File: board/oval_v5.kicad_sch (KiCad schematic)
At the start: 131 parts, among them J1 HDR-5x1, J10 HDR-4x1, J11 HDR-4x1, J12 HDR-4x1, J13 HDR-4x1, J14 HDR-4x1, J15 HDR-4x1, J16 HDR-4x1, J17 HDR-4x1, J18 Conn_Coaxial, J19 Conn_01x02, J2 HDR-4x1, J20 Conn_01x02, J21 Conn_02x02_Counter_Clockwise, J22 HDR-2x1, J23 HDR-2x1, J25 Conn_01x06, J3 HDR-4x1, J4 Conn_01x06, J5 Micro_SD_Card, J6 Conn_01x02, J7 HDR-4x1, J8 Conn_01x08, J9 HDR-4x1, P1 USB_C_Plug_USB2.0, Q1 Q_PMOS_GSD, Q2 MMBT3904, Q3 MMBT3904, SW1 SW_DIP_x02, SW2 SW_DIP_x02, U1 RV-8803, U10 SiP32431DR3, U11 SiP32431DR3, U12 SiP32431DR3, U13 SiP32431DR3, U14 SiP32431DR3, U16 PCA9548APW, U17 SiP32431DR3, U18 PCA9555PW, U2 ESP32-S3-WROOM-1, U3 TMP117xxDRV, U4 RFM95W-915S2, U7 MAX3485, U8 AP7361C-33E, U9 AP7361C-33E

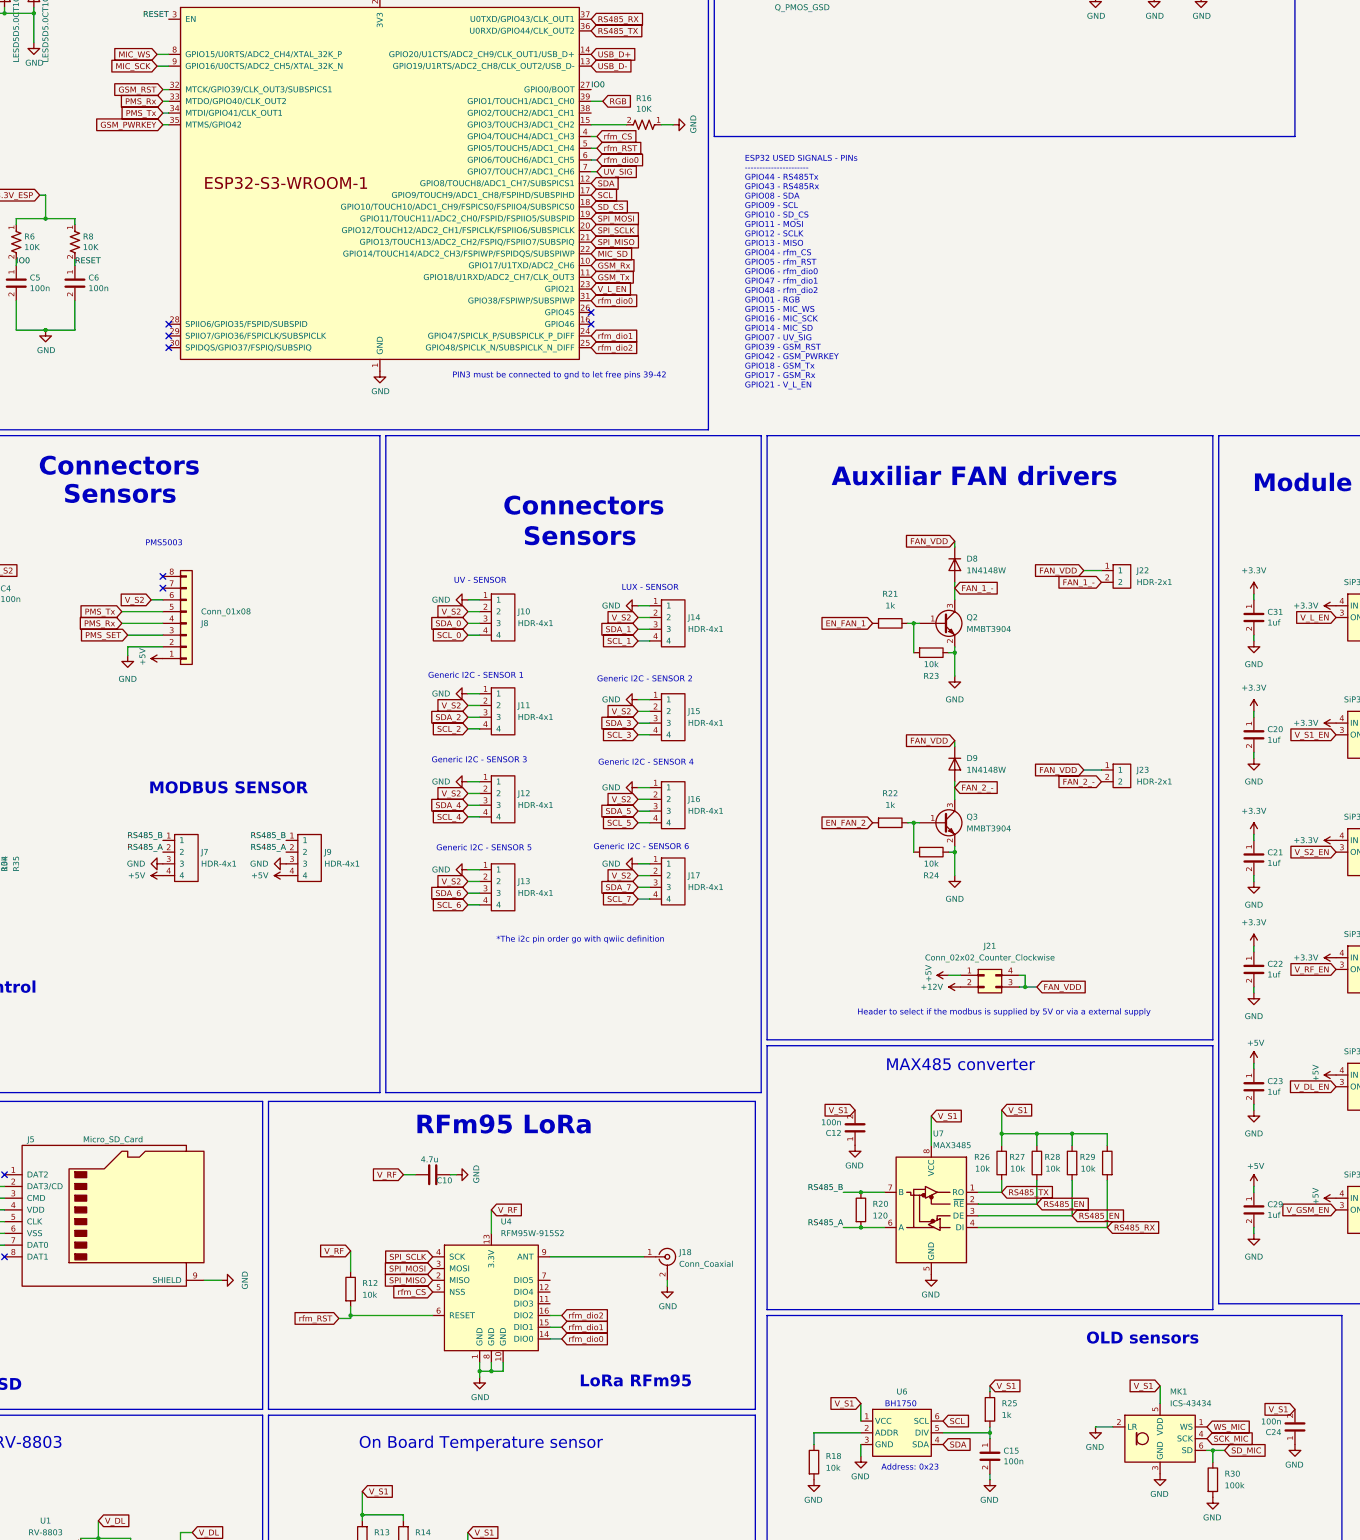
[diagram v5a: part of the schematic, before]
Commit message: routing pads
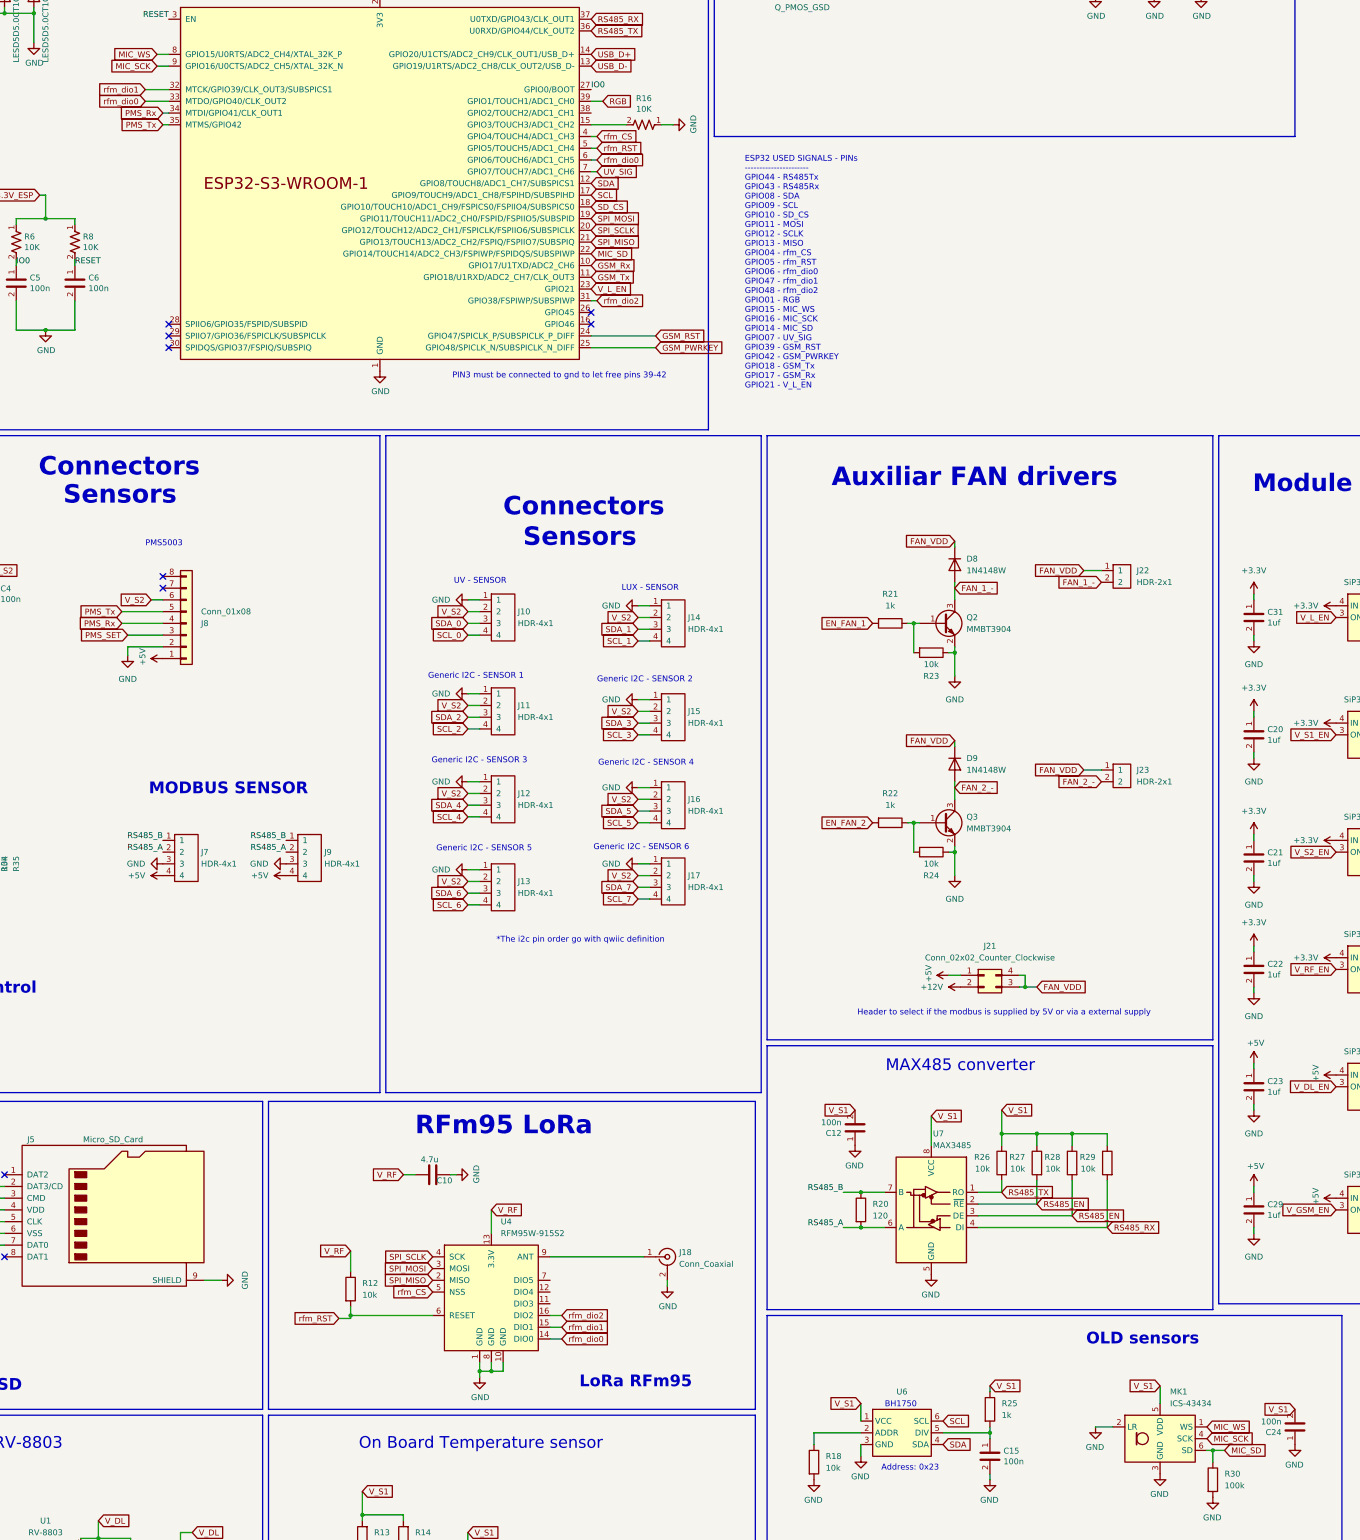
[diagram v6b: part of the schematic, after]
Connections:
- net SCK_MIC is gone; now on net MIC_SCK: MK1.4 (SCK)
- net SD_MIC is gone; now on net MIC_SD: MK1.6 (SD), R30.1
- net WS_MIC is gone; now on net MIC_WS: MK1.1 (WS)
- net GSM_PWRKEY: now also U2.25 (GPIO48/SPICLK_N/SUBSPICLK_N_DIFF); no longer U2.35 (MTMS/GPIO42)
- net GSM_RST: now also U2.24 (GPIO47/SPICLK_P/SUBSPICLK_P_DIFF); no longer U2.32 (MTCK/GPIO39/CLK_OUT3/SUBSPICS1)
- net PMS_Rx: now also U2.34 (MTDI/GPIO41/CLK_OUT1); no longer U2.33 (MTDO/GPIO40/CLK_OUT2)
- net PMS_Tx: now also U2.35 (MTMS/GPIO42); no longer U2.34 (MTDI/GPIO41/CLK_OUT1)
- net rfm_dio0: now also U2.33 (MTDO/GPIO40/CLK_OUT2); no longer U2.31 (GPIO38/FSPIWP/SUBSPIWP)
- net rfm_dio1: now also U2.32 (MTCK/GPIO39/CLK_OUT3/SUBSPICS1); no longer U2.24 (GPIO47/SPICLK_P/SUBSPICLK_P_DIFF)
- net rfm_dio2: now also U2.31 (GPIO38/FSPIWP/SUBSPIWP); no longer U2.25 (GPIO48/SPICLK_N/SUBSPICLK_N_DIFF)
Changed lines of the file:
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@@
 	(wire
 		(pts
-			(xy 95.25 93.98) (xy 96.52 93.98)
+			(xy 91.44 93.98) (xy 96.52 93.98)
 		)
 		(stroke
@@
 	(wire
 		(pts
+			(xy 187.96 144.78) (xy 201.93 144.78)
+		)
+		(stroke
+			(width 0)
+			(type default)
+		)
+	)
+	(wire
+		(pts
 			(xy 31.75 392.43) (xy 31.75 389.89)
 		)
@@
 	(wire
 		(pts
+			(xy 189.23 137.16) (xy 187.96 137.16)
+		)
+		(stroke
+			(width 0)
+			(type default)
+		)
+	)
+	(wire
+		(pts
 			(xy 331.47 302.26) (xy 331.47 303.53)
 		)
@@
 	(wire
 		(pts
+			(xy 187.96 147.32) (xy 201.93 147.32)
+		)
+		(stroke
+			(width 0)
+			(type default)
+		)
+	)
+	(wire
+		(pts
 			(xy 93.98 83.82) (xy 96.52 83.82)
 		)
@@
 	(wire
 		(pts
-			(xy 95.25 91.44) (xy 96.52 91.44)
+			(xy 91.44 91.44) (xy 96.52 91.44)
 		)
 		(stroke
@@
 		)
 	)
-	(global_label "V_DL"
+	(global_label "rfm_dio1"
 		(shape input)
-		(at 81.28 401.32 0)
+		(at 91.44 91.44 180)
 		(fields_autoplaced yes)
 		(effects
@@
 				(size 1.27 1.27)
 			)
-			(justify left)
+			(justify right)
 		)
 		(property "Intersheetrefs" "${INTERSHEET_REFS}"
-			(at 88.6195 401.32 0)
+			(at 80.1697 91.44 0)
 			(effects
 				(font
 					(size 1.27 1.27)
 				)
-				(justify left)
+				(justify right)
 				(hide yes)
 			)
 		)
 	)
-	(global_label "rfm_dio0"
+	(global_label "V_DL"
 		(shape input)
-		(at 187.96 137.16 0)
+		(at 81.28 401.32 0)
 		(fields_autoplaced yes)
 		(effects
@@
 		)
 		(property "Intersheetrefs" "${INTERSHEET_REFS}"
-			(at 199.2303 137.16 0)
+			(at 88.6195 401.32 0)
 			(effects
 				(font
@@
 		)
 	)
-	(global_label "SCK_MIC"
+	(global_label "MIC_SCK"
 		(shape input)
 		(at 321.31 383.54 0)
@@
 		)
 	)
+	(global_label "PMS_Rx"
+		(shape input)
+		(at 95.25 96.52 180)
+		(fields_autoplaced yes)
+		(effects
+			(font
+				(size 1.27 1.27)
+			)
+			(justify right)
+		)
+		(property "Intersheetrefs" "${INTERSHEET_REFS}"
+			(at 85.0682 96.52 0)
+			(effects
+				(font
+					(size 1.27 1.27)
+				)
+				(justify right)
+				(hide yes)
+			)
+		)
+	)
 	(global_label "V_S1"
 		(shape input)
@@
 		)
 	)
-	(global_label "GSM_RST"
-		(shape input)
-		(at 95.25 91.44 180)
-		(fields_autoplaced yes)
-		(effects
-			(font
-				(size 1.27 1.27)
-			)
-			(justify right)
-		)
-		(property "Intersheetrefs" "${INTERSHEET_REFS}"
-			(at 83.9192 91.44 0)
-			(effects
-				(font
-					(size 1.27 1.27)
-				)
-				(justify right)
-				(hide yes)
-			)
-		)
-	)
 	(global_label "FAN_1_-"
 		(shape input)
@@
 		)
 	)
-	(global_label "PMS_Rx"
-		(shape input)
-		(at 95.25 93.98 180)
-		(fields_autoplaced yes)
-		(effects
-			(font
-				(size 1.27 1.27)
-			)
-			(justify right)
-		)
-		(property "Intersheetrefs" "${INTERSHEET_REFS}"
-			(at 85.0682 93.98 0)
-			(effects
-				(font
-					(size 1.27 1.27)
-				)
-				(justify right)
-				(hide yes)
-			)
-		)
-	)
 	(global_label "RGB"
 		(shape input)
@@
 		)
 	)
-	(global_label "WS_MIC"
+	(global_label "MIC_WS"
 		(shape input)
 		(at 321.31 381 0)
@@
 		)
 	)
+	(global_label "PMS_Tx"
+		(shape input)
+		(at 95.25 99.06 180)
+		(fields_autoplaced yes)
+		(effects
+			(font
+				(size 1.27 1.27)
+			)
+			(justify right)
+		)
+		(property "Intersheetrefs" "${INTERSHEET_REFS}"
+			(at 85.3706 99.06 0)
+			(effects
+				(font
+					(size 1.27 1.27)
+				)
+				(justify right)
+				(hide yes)
+			)
+		)
+	)
 	(global_label "SCL"
 		(shape input)
@@
 		)
 	)
+	(global_label "GSM_RST"
+		(shape input)
+		(at 201.93 144.78 0)
+		(fields_autoplaced yes)
+		(effects
+			(font
+				(size 1.27 1.27)
+			)
+			(justify left)
+		)
+		(property "Intersheetrefs" "${INTERSHEET_REFS}"
+			(at 213.2608 144.78 0)
+			(effects
+				(font
+					(size 1.27 1.27)
+				)
+				(justify left)
+				(hide yes)
+			)
+		)
+	)
 	(global_label "rfm_dio1"
 		(shape input)
@@
 		)
 	)
+	(global_label "GSM_PWRKEY"
+		(shape input)
+		(at 201.93 147.32 0)
+		(fields_autoplaced yes)
+		(effects
+			(font
+				(size 1.27 1.27)
+			)
+			(justify left)
+		)
+		(property "Intersheetrefs" "${INTERSHEET_REFS}"
+			(at 217.3127 147.32 0)
+			(effects
+				(font
+					(size 1.27 1.27)
+				)
+				(justify left)
+				(hide yes)
+			)
+		)
+	)
 	(global_label "SCL"
 		(shape input)
@@
 		)
 	)
-	(global_label "rfm_dio1"
-		(shape input)
-		(at 187.96 144.78 0)
-		(fields_autoplaced yes)
-		(effects
-			(font
-				(size 1.27 1.27)
-			)
-			(justify left)
-		)
-		(property "Intersheetrefs" "${INTERSHEET_REFS}"
-			(at 199.2303 144.78 0)
-			(effects
-				(font
-					(size 1.27 1.27)
-				)
-				(justify left)
-				(hide yes)
-			)
-		)
-	)
 	(global_label "SDA"
 		(shape input)
@@
 		)
 	)
-	(global_label "rfm_dio2"
-		(shape input)
-		(at 187.96 147.32 0)
-		(fields_autoplaced yes)
-		(effects
-			(font
-				(size 1.27 1.27)
-			)
-			(justify left)
-		)
-		(property "Intersheetrefs" "${INTERSHEET_REFS}"
-			(at 199.2303 147.32 0)
-			(effects
-				(font
-					(size 1.27 1.27)
-				)
-				(justify left)
-				(hide yes)
-			)
-		)
-	)
 	(global_label "SDA_5"
 		(shape input)
@@
 		)
 	)
-	(global_label "SD_MIC"
+	(global_label "MIC_SD"
 		(shape input)
 		(at 325.12 386.08 0)
@@
 		)
 	)
-	(global_label "V_RF"
+	(global_label "rfm_dio0"
 		(shape input)
-		(at 375.92 276.86 0)
+		(at 91.44 93.98 180)
 		(fields_autoplaced yes)
 		(effects
@@
 				(size 1.27 1.27)
 			)
-			(justify left)
+			(justify right)
 		)
 		(property "Intersheetrefs" "${INTERSHEET_REFS}"
-			(at 383.32 276.86 0)
+			(at 80.1697 93.98 0)
 			(effects
 				(font
 					(size 1.27 1.27)
 				)
-				(justify left)
+				(justify right)
 				(hide yes)
 			)
 		)
 	)
-	(global_label "V_S2"
+	(global_label "V_RF"
 		(shape input)
-		(at 161.29 204.47 180)
+		(at 375.92 276.86 0)
 		(fields_autoplaced yes)
 		(effects
@@
 				(size 1.27 1.27)
 			)
-			(justify right)
+			(justify left)
 		)
 		(property "Intersheetrefs" "${INTERSHEET_REFS}"
-			(at 153.8296 204.47 0)
+			(at 383.32 276.86 0)
 			(effects
 				(font
 					(size 1.27 1.27)
 				)
-				(justify right)
+				(justify left)
 				(hide yes)
 			)
 		)
 	)
-	(global_label "PMS_Tx"
+	(global_label "V_S2"
 		(shape input)
-		(at 95.25 96.52 180)
+		(at 161.29 204.47 180)
 		(fields_autoplaced yes)
 		(effects
@@
 		)
 		(property "Intersheetrefs" "${INTERSHEET_REFS}"
-			(at 85.3706 96.52 0)
+			(at 153.8296 204.47 0)
 			(effects
 				(font
@@
 		)
 	)
+	(global_label "rfm_dio2"
+		(shape input)
+		(at 189.23 137.16 0)
+		(fields_autoplaced yes)
+		(effects
+			(font
+				(size 1.27 1.27)
+			)
+			(justify left)
+		)
+		(property "Intersheetrefs" "${INTERSHEET_REFS}"
+			(at 200.5003 137.16 0)
+			(effects
+				(font
+					(size 1.27 1.27)
+				)
+				(justify left)
+				(hide yes)
+			)
+		)
+	)
 	(global_label "V_DL"
 		(shape input)
@@
 				(hide yes)
 			)
-		)
-	)
-	(global_label "GSM_PWRKEY"
-		(shape input)
-		(at 95.25 99.06 180)
-		(fields_autoplaced yes)
-		(effects
-			(font
-				(size 1.27 1.27)
-			)
-			(justify right)
-		)
-		(property "Intersheetrefs" "${INTERSHEET_REFS}"
-			(at 79.8673 99.06 0)
-			(effects
-				(font
-					(size 1.27 1.27)
-				)
-				(justify right)
-				(hide yes)
-			)

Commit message: i2c multiplexer routed
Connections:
- net SCL_0: now also J17.4; no longer J10.4
- net SCL_1: now also J16.4; no longer J14.4
- net SCL_2: now also J10.4; no longer J11.4
- net SCL_3: now also J11.4; no longer J15.4
- net SCL_4: now also J13.4; no longer J12.4
- net SCL_5: now also J12.4; no longer J16.4
- net SCL_6: now also J14.4; no longer J13.4
- net SCL_7: now also J15.4; no longer J17.4
- net SDA_0: now also J17.3; no longer J10.3
- net SDA_1: now also J16.3; no longer J14.3
- net SDA_2: now also J10.3; no longer J11.3
- net SDA_3: now also J11.3; no longer J15.3
- net SDA_4: now also J13.3; no longer J12.3
- net SDA_5: now also J12.3; no longer J16.3
- net SDA_6: now also J14.3; no longer J13.3
- net SDA_7: now also J15.3; no longer J17.3
- net I2C_BUS_RST: now reaches R31.2, U16.3 (~{RESET})
- net I2C_BUS_RST: now also U18.15 (IO1_2)
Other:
- note added: "Expansor GPIO ------------------- GPIO00 - onBoardLED GPIO01 - V_GSM_EN GPIO02 - V_S1_EN GPIO03 - V_S2_EN GPIO04 - V_RF_EN GPIO05 - V_DL_EN GPIO06 - FAN_1_EN GPIO07 - FAN_1_EN GPIO08 - PMS_SET GPIO09 - RS485_EN GPIO10 - I2C_BUS_RST"
- note removed: "Expansor GPIO ------------------- GPIO00 - onBoardLED GPIO01 - V_GSM_EN GPIO02 - V_S1_EN GPIO03 - V_S2_EN GPIO04 - V_RF_EN GPIO05 - V_DL_EN GPIO06 - FAN_1_EN GPIO07 - FAN_1_EN GPIO08 - PMS_SET GPIO09 - RS485_EN"

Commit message: i2c adding pull up resistors
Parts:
- added R38, R39, R40, R41, R42, R43, R44, R45, R46, R47, R48, R49, R50, R51, R52, R53: 10K, Resistor_SMD:R_0603_1608Metric, symbol IoWLabs:RES
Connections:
- net SCL_0: now also R53.1
- net SCL_1: now also R51.1
- net SCL_2: now also R39.1
- net SCL_3: now also R41.1
- net SCL_4: now also R45.1
- net SCL_5: now also R43.1
- net SCL_6: now also R47.1
- net SCL_7: now also R49.1
- net SDA_0: now also R52.1
- net SDA_1: now also R50.1
- net SDA_2: now also R38.1
- net SDA_3: now also R40.1
- net SDA_4: now also R44.1
- net SDA_5: now also R42.1
- net SDA_6: now also R46.1
- net SDA_7: now also R48.1
- net V_S2: now also R38.2, R39.2, R40.2, R41.2, R42.2, R43.2, R44.2, R45.2, R46.2, R47.2, R48.2, R49.2, R50.2, R51.2, R52.2, R53.2
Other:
- note added: "*The i2c pin order go with DF ROBOT definition. **The connectors use 4x1 JST PH 2.0 pitch connectors"
- note added: "Gas sensors i2c connectors"
- note removed: "*The i2c pin order go with qwiic definition"
- moved on the sheet: J10, J11, J12, J13, J14, J15, J16, J17
